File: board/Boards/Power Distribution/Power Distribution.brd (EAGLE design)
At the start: 48.2 x 84.8 mm, 24 parts

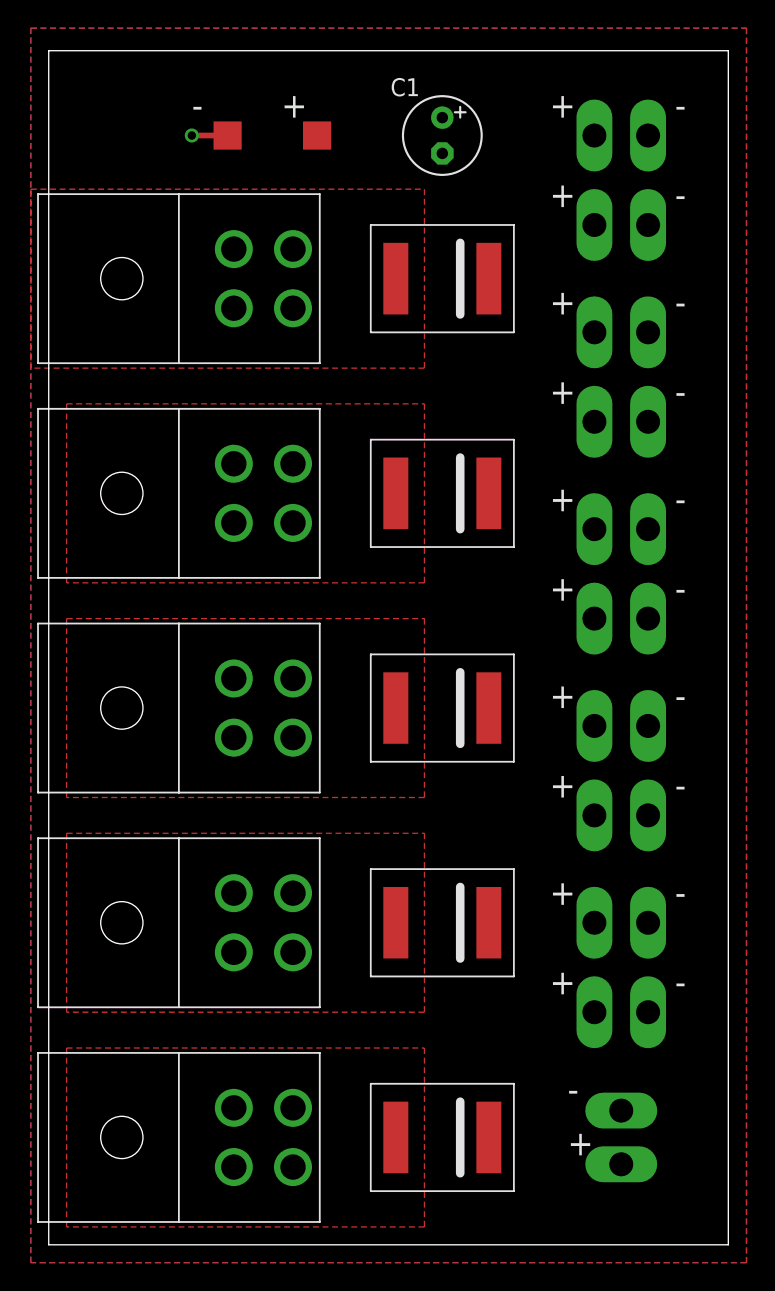
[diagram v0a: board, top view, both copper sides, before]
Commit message: consolidated parts
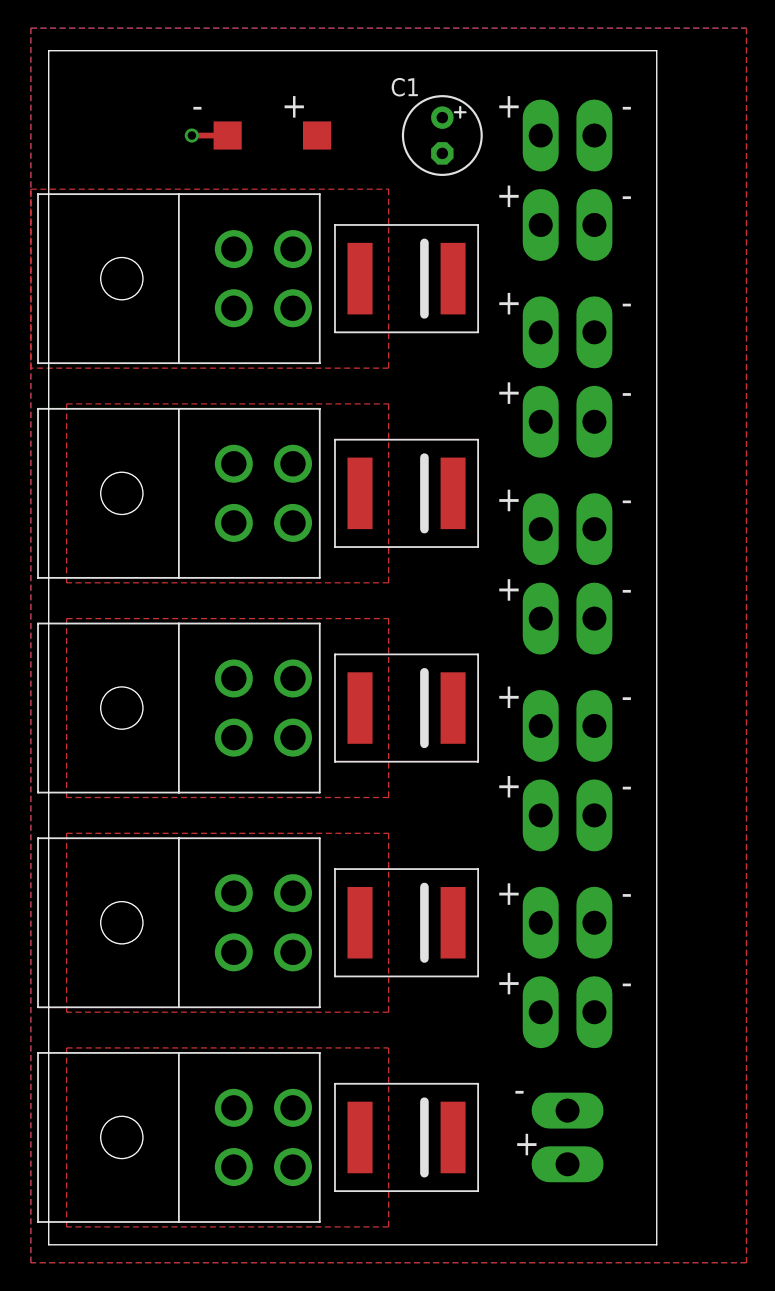
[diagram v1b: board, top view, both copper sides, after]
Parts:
- moved TP1 3.81 mm to (36.8, 7.62)
- moved TP10 3.81 mm to (36.8, 50.8)
- moved TP11 3.81 mm to (36.8, 36.8)
- moved TP2 3.81 mm to (36.8, 16.5)
- moved TP3 3.81 mm to (36.8, 22.9)
- moved TP4 3.81 mm to (36.8, 72.4)
- moved TP5 3.81 mm to (36.8, 58.4)
- moved TP6 3.81 mm to (36.8, 44.5)
- moved TP7 3.81 mm to (36.8, 30.5)
- moved TP8 3.81 mm to (36.8, 78.7)
- moved TP9 3.81 mm to (36.8, 64.8)
- moved U$10 2.54 mm to (25.4, 68.6)
- moved U$6 2.54 mm to (25.4, 7.62)
- moved U$7 2.54 mm to (25.4, 22.9)
- moved U$8 2.54 mm to (25.4, 38.1)
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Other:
- board size 48.2 x 84.8 mm -> 43.2 x 84.8 mm

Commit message: board is smaller again
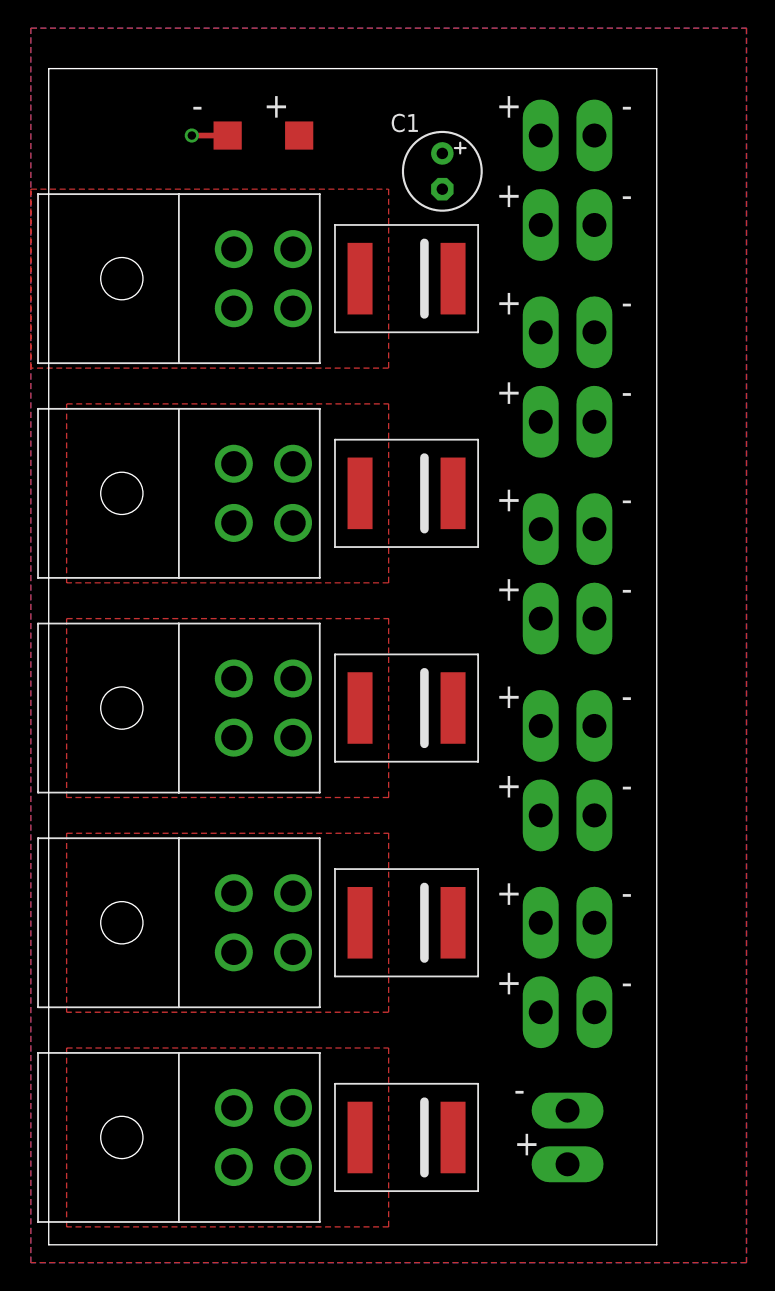
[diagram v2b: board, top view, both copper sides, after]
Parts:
- moved C1 2.54 mm to (27.9, 76.2)
- moved TP12 1.27 mm to (17.8, 78.7)
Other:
- board size 43.2 x 84.8 mm -> 43.2 x 83.5 mm
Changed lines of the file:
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@@
 <plain>
 <wire x1="0" y1="0" x2="43.16" y2="0" width="0" layer="20"/>
-<wire x1="43.16" y1="0" x2="43.16" y2="84.76" width="0" layer="20"/>
-<wire x1="43.16" y1="84.76" x2="0" y2="84.76" width="0" layer="20"/>
-<wire x1="0" y1="84.76" x2="0" y2="0" width="0" layer="20"/>
+<wire x1="43.16" y1="0" x2="43.16" y2="83.49" width="0" layer="20"/>
+<wire x1="43.16" y1="83.49" x2="0" y2="83.49" width="0" layer="20"/>
+<wire x1="0" y1="83.49" x2="0" y2="0" width="0" layer="20"/>
 <text x="31.75" y="80.01" size="1.778" layer="21">+</text>
 <text x="31.75" y="73.66" size="1.778" layer="21">+</text>
@@
 <text x="33.02" y="10.16" size="1.778" layer="21">-</text>
 <text x="10.16" y="80.01" size="1.778" layer="21">-</text>
-<text x="16.51" y="80.01" size="1.778" layer="21">+</text>
+<text x="15.24" y="80.01" size="1.778" layer="21">+</text>
 <text x="25.4" y="6.35" size="1.778" layer="22" rot="MR90">hitchBOT Power Distribution Board
 C.G &amp; D.K
@@
 <attribute name="TP_SIGNAL_NAME" value="" x="34.29" y="31.115" size="1" layer="37"/>
 </element>
-<element name="C1" library="resistor" package="E2,5-6" value="" x="27.94" y="78.74" smashed="yes" rot="R270">
-<attribute name="NAME" x="24.257" y="81.534" size="1.27" layer="25" ratio="10"/>
-<attribute name="VALUE" x="25.273" y="76.073" size="1.27" layer="27" ratio="10" rot="R270"/>
-</element>
-<element name="TP12" library="testpad" package="TP20SQ" value="TPTP20SQ" x="19.05" y="78.74" smashed="yes">
-<attribute name="TP_SIGNAL_NAME" value="" x="19.05" y="76.2" size="1" layer="37"/>
-<attribute name="VALUE" x="18.034" y="77.597" size="0.0254" layer="27"/>
+<element name="C1" library="resistor" package="E2,5-6" value="" x="27.94" y="76.2" smashed="yes" rot="R270">
+<attribute name="NAME" x="24.257" y="78.994" size="1.27" layer="25" ratio="10"/>
+<attribute name="VALUE" x="25.273" y="73.533" size="1.27" layer="27" ratio="10" rot="R270"/>
+</element>
+<element name="TP12" library="testpad" package="TP20SQ" value="TPTP20SQ" x="17.78" y="78.74" smashed="yes">
+<attribute name="TP_SIGNAL_NAME" value="" x="17.78" y="76.2" size="1" layer="37"/>
+<attribute name="VALUE" x="16.764" y="77.597" size="0.0254" layer="27"/>
 </element>
 <element name="TP13" library="testpad" package="TP20SQ" value="TPTP20SQ" x="12.7" y="78.74" smashed="yes">

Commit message: updated power dist. board + created a micro version
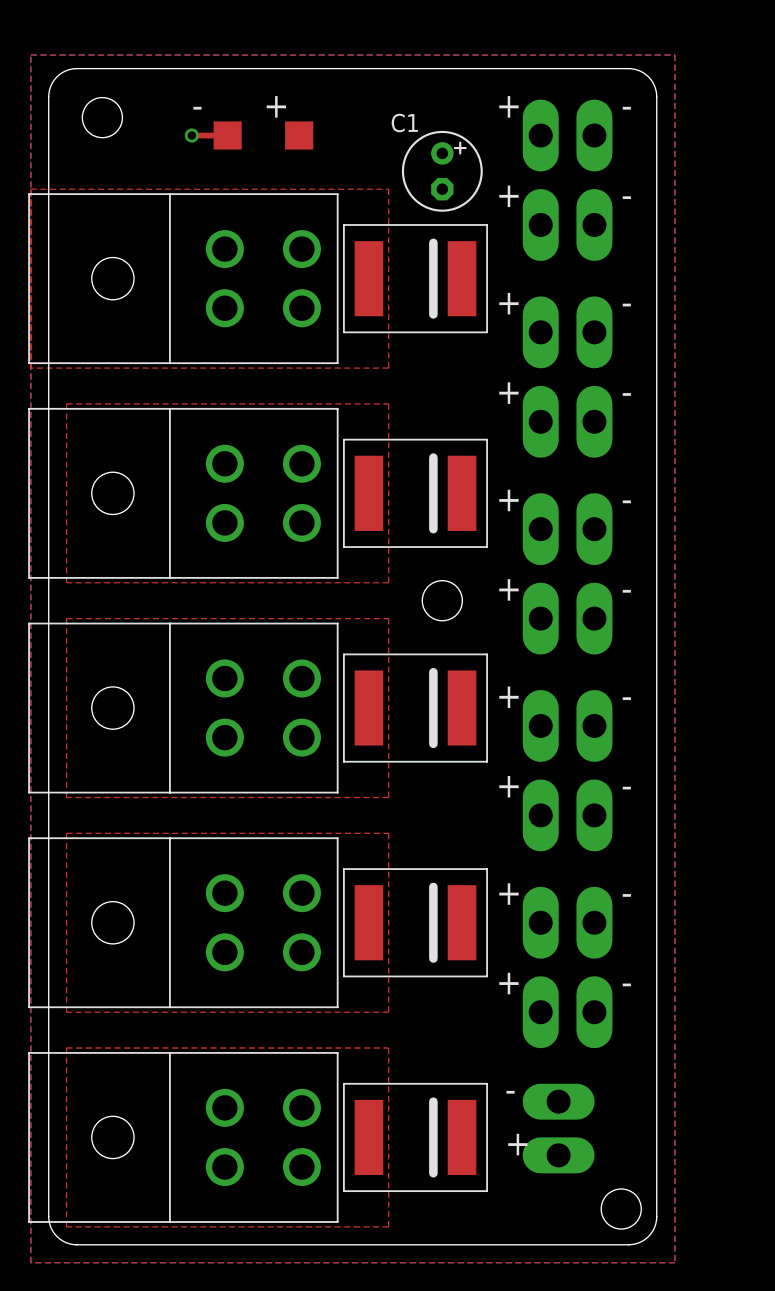
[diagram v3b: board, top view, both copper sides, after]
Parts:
- moved TP1 0.90 mm to (36.2, 8.26)
- moved U$10 0.64 mm to (26.0, 68.6)
- moved U$6 0.64 mm to (26.0, 7.62)
- moved U$7 0.64 mm to (26.0, 22.9)
- moved U$8 0.64 mm to (26.0, 38.1)
- moved U$9 0.64 mm to (26.0, 53.3)
- moved U$1 0.63 mm to (14.6, 22.9)
- moved U$2 0.63 mm to (14.6, 38.1)
- moved U$3 0.63 mm to (14.6, 53.3)
- moved U$4 0.63 mm to (14.6, 68.6)
- moved U$5 0.63 mm to (14.6, 7.62)
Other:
- outline, holes or cut-outs redrawn
- board text added: "hitchBOT Power Distribution Board C.G & D.K & R.E & D.B v1.1 - June 2015"
- board text removed: "hitchBOT Power Distribution Board C.G & D.K v1.0 - August 2014"
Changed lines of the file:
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@@
 <setting verticaltext="up"/>
 </settings>
-<grid distance="0.05" unitdist="inch" unit="inch" style="lines" multiple="1" display="no" altdistance="0.025" altunitdist="inch" altunit="inch"/>
+<grid distance="0.025" unitdist="inch" unit="inch" style="lines" multiple="1" display="no" altdistance="0.025" altunitdist="inch" altunit="inch"/>
 <layers>
 <layer number="1" name="Top" color="4" fill="1" visible="yes" active="yes"/>
@@
 <layer number="43" name="vRestrict" color="2" fill="10" visible="yes" active="yes"/>
 <layer number="44" name="Drills" color="7" fill="1" visible="no" active="yes"/>
-<layer number="45" name="Holes" color="7" fill="1" visible="no" active="yes"/>
+<layer number="45" name="Holes" color="7" fill="1" visible="yes" active="yes"/>
 <layer number="46" name="Milling" color="3" fill="1" visible="no" active="yes"/>
 <layer number="47" name="Measures" color="7" fill="1" visible="no" active="yes"/>
@@
 <board>
 <plain>
-<wire x1="0" y1="0" x2="43.16" y2="0" width="0" layer="20"/>
-<wire x1="43.16" y1="0" x2="43.16" y2="83.49" width="0" layer="20"/>
-<wire x1="43.16" y1="83.49" x2="0" y2="83.49" width="0" layer="20"/>
-<wire x1="0" y1="83.49" x2="0" y2="0" width="0" layer="20"/>
+<wire x1="0" y1="81.49" x2="0" y2="2" width="0" layer="20"/>
+<wire x1="0" y1="2" x2="2" y2="0" width="0" layer="20" curve="90"/>
+<wire x1="2" y1="0" x2="41.16" y2="0" width="0" layer="20"/>
+<wire x1="41.16" y1="0" x2="43.16" y2="2" width="0" layer="20" curve="90"/>
+<wire x1="43.16" y1="2" x2="43.16" y2="81.49" width="0" layer="20"/>
+<wire x1="43.16" y1="81.49" x2="41.16" y2="83.49" width="0" layer="20" curve="90"/>
+<wire x1="41.16" y1="83.49" x2="2" y2="83.49" width="0" layer="20"/>
+<wire x1="2" y1="83.49" x2="0" y2="81.49" width="0" layer="20" curve="90"/>
 <text x="31.75" y="80.01" size="1.778" layer="21">+</text>
 <text x="31.75" y="73.66" size="1.778" layer="21">+</text>
@@
 <text x="31.75" y="24.13" size="1.778" layer="21">+</text>
 <text x="31.75" y="17.78" size="1.778" layer="21">+</text>
-<text x="33.02" y="6.35" size="1.778" layer="21">+</text>
+<text x="32.385" y="6.35" size="1.778" layer="21">+</text>
 <text x="40.64" y="17.78" size="1.778" layer="21">-</text>
 <text x="40.64" y="24.13" size="1.778" layer="21">-</text>
@@
 <text x="40.64" y="73.66" size="1.778" layer="21">-</text>
 <text x="40.64" y="80.01" size="1.778" layer="21">-</text>
-<text x="33.02" y="10.16" size="1.778" layer="21">-</text>
+<text x="32.385" y="10.16" size="1.778" layer="21">-</text>
 <text x="10.16" y="80.01" size="1.778" layer="21">-</text>
 <text x="15.24" y="80.01" size="1.778" layer="21">+</text>
-<text x="25.4" y="6.35" size="1.778" layer="22" rot="MR90">hitchBOT Power Distribution Board
-C.G &amp; D.K
-v1.0 - August 2014</text>
+<text x="25.4" y="5.08" size="1.778" layer="22" rot="MR90">hitchBOT Power Distribution Board
+C.G &amp; D.K &amp; R.E &amp; D.B
+v1.1 - June 2015</text>
+<hole x="3.81" y="80.01" drill="2.8448"/>
+<hole x="40.64" y="2.54" drill="2.8448"/>
+<hole x="27.94" y="45.72" drill="2.8448"/>
 </plain>
 <attributes>
@@
 </autorouter>
 <elements>
-<element name="U$1" library="Molex" package="2X2MOLEX" value="2X2-MOLEX" x="15.24" y="22.86" rot="R270"/>
-<element name="U$2" library="Molex" package="2X2MOLEX" value="2X2-MOLEX" x="15.24" y="38.1" rot="R270"/>
-<element name="U$3" library="Molex" package="2X2MOLEX" value="2X2-MOLEX" x="15.24" y="53.34" rot="R270"/>
-<element name="U$4" library="Molex" package="2X2MOLEX" value="2X2-MOLEX" x="15.24" y="68.58" rot="R270"/>
-<element name="U$5" library="Molex" package="2X2MOLEX" value="2X2-MOLEX" x="15.24" y="7.62" rot="R270"/>
-<element name="U$6" library="Diodes" package="DO-214AB" value="DO-214AB" x="25.4" y="7.62"/>
-<element name="U$7" library="Diodes" package="DO-214AB" value="DO-214AB" x="25.4" y="22.86"/>
-<element name="U$8" library="Diodes" package="DO-214AB" value="DO-214AB" x="25.4" y="38.1"/>
-<element name="U$9" library="Diodes" package="DO-214AB" value="DO-214AB" x="25.4" y="53.34"/>
-<element name="U$10" library="Diodes" package="DO-214AB" value="DO-214AB" x="25.4" y="68.58"/>
-<element name="TP1" library="testpad" package="P2-38-17" value="TP2P2-38-17" x="36.83" y="7.62" smashed="yes" rot="R90">
-<attribute name="TP_SIGNAL_NAME" value="" x="42.545" y="5.08" size="1" layer="37" rot="R90"/>
+<element name="U$1" library="Molex" package="2X2MOLEX" value="2X2-MOLEX" x="14.605" y="22.86" rot="R270"/>
+<element name="U$2" library="Molex" package="2X2MOLEX" value="2X2-MOLEX" x="14.605" y="38.1" rot="R270"/>
+<element name="U$3" library="Molex" package="2X2MOLEX" value="2X2-MOLEX" x="14.605" y="53.34" rot="R270"/>
+<element name="U$4" library="Molex" package="2X2MOLEX" value="2X2-MOLEX" x="14.605" y="68.58" rot="R270"/>
+<element name="U$5" library="Molex" package="2X2MOLEX" value="2X2-MOLEX" x="14.605" y="7.62" rot="R270"/>
+<element name="U$6" library="Diodes" package="DO-214AB" value="DO-214AB" x="26.035" y="7.62"/>
+<element name="U$7" library="Diodes" package="DO-214AB" value="DO-214AB" x="26.035" y="22.86"/>
+<element name="U$8" library="Diodes" package="DO-214AB" value="DO-214AB" x="26.035" y="38.1"/>
+<element name="U$9" library="Diodes" package="DO-214AB" value="DO-214AB" x="26.035" y="53.34"/>
+<element name="U$10" library="Diodes" package="DO-214AB" value="DO-214AB" x="26.035" y="68.58"/>
+<element name="TP1" library="testpad" package="P2-38-17" value="TP2P2-38-17" x="36.195" y="8.255" smashed="yes" rot="R90">
+<attribute name="TP_SIGNAL_NAME" value="" x="41.91" y="5.715" size="1" layer="37" rot="R90"/>
 </element>
 <element name="TP2" library="testpad" package="P2-38-17" value="TP2P2-38-17" x="36.83" y="16.51" smashed="yes">
@@
 <contactref element="TP10" pad="TP-2"/>
 <polygon width="0.4064" layer="16" isolate="0.4064" thermals="no">
-<vertex x="-1.27" y="86.36"/>
-<vertex x="49.53" y="86.36"/>
-<vertex x="49.53" y="-1.27"/>
+<vertex x="-1.27" y="84.455"/>
+<vertex x="44.45" y="84.455"/>
+<vertex x="44.45" y="-1.27"/>
 <vertex x="-1.27" y="-1.27"/>
 </polygon>
@@
 <contactref element="TP10" pad="TP-1"/>
 <polygon width="0.4064" layer="1" isolate="0.4064" thermals="no" rank="2">
-<vertex x="-1.27" y="86.36"/>
-<vertex x="49.53" y="86.36"/>
-<vertex x="49.53" y="-1.27"/>
+<vertex x="-1.27" y="84.455"/>
+<vertex x="44.45" y="84.455"/>
+<vertex x="44.45" y="-1.27"/>
 <vertex x="-1.27" y="-1.27"/>
 </polygon>
